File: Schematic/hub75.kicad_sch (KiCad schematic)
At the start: 3 parts, among them J1 Conn_02x08_Odd_Even, J3 Conn_01x04_Pin, U1 74LS08

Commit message: initial CB design
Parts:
- added C6: .1uF, Capacitor_SMD:C_0805_2012Metric_Pad1.18x1.45mm_HandSolder, symbol Device:C
- added LD1: LED_Green, LED_THT:LED_D5.0mm, symbol stm32f091-rescue:LED_Small_ALT-Device
- added R1: 5.1k, Resistor_SMD:R_1206_3216Metric_Pad1.30x1.75mm_HandSolder, symbol Device:R_US
- added R16, R18, R20, R21, R22, R24, R25, R26, R27, R28, R29, R30, R31, R32, R33, R34, R35, R36, R37, R38, R39: 1k, Resistor_SMD:R_1206_3216Metric_Pad1.30x1.75mm_HandSolder, symbol Device:R
- added R17, R19, R23: 0, Resistor_SMD:R_1206_3216Metric_Pad1.30x1.75mm_HandSolder, symbol Device:R
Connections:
- net +3V0: now also C6.1
- net GND: now also C6.2, LD1.1 (K), R17.2, R19.2, R23.2, R34.1, R35.1, R36.1, R37.1, R38.1, R39.1; no longer J1.16 (Pin_16), J1.4 (Pin_4), J1.8 (Pin_8), U1.10, U1.12, U1.13, U1.4, U1.5, U1.9
- net PC0: now also R24.2; no longer J1.1 (Pin_1)
- net PC1: now also R16.2; no longer J1.2 (Pin_2)
- net PC10: now also R29.2; no longer J1.11 (Pin_11)
- net PC11: now also R21.2; no longer J1.12 (Pin_12)
- net PC12: now also R22.2; no longer J1.14 (Pin_14)
- net PC13: now also R31.2; no longer J1.15 (Pin_15)
- net PC2: now also R25.2; no longer J1.3 (Pin_3)
- net PC3: now also R26.2; no longer J1.5 (Pin_5)
- net PC4: now also R18.2; no longer J1.6 (Pin_6)
- net PC5: now also R27.2; no longer J1.7 (Pin_7)
- net PC6: now also R33.1; no longer U1.2
- net PC7: now also R32.1; no longer U1.1
- net PC8: now also R28.2; no longer J1.9 (Pin_9)
- net PC9: now also R20.2; no longer J1.10 (Pin_10)
- net at J1.13 (Pin_13): now also R30.1; no longer U1.3
- new net: R37.2, U1.10
- new net: R36.2, U1.9
- new net: J1.15 (Pin_15), R31.1
- new net: R32.2, U1.1
- new net: J1.3 (Pin_3), R25.1
- new net: J1.6 (Pin_6), R18.1
- new net: J1.16 (Pin_16), R23.1
- new net: R1.1, R30.2, U1.3
- new net: R38.2, U1.12
- new net: R33.2, U1.2
- new net: LD1.2 (A), R1.2
- new net: J1.7 (Pin_7), R27.1
- new net: R34.2, U1.4
- new net: R35.2, U1.5
- new net: J1.14 (Pin_14), R22.1
- new net: J1.2 (Pin_2), R16.1
- new net: R39.2, U1.13
- new net: J1.11 (Pin_11), R29.1
- new net: J1.9 (Pin_9), R28.1
- new net: J1.12 (Pin_12), R21.1
- new net: J1.1 (Pin_1), R24.1
- new net: J1.10 (Pin_10), R20.1
- new net: J1.4 (Pin_4), R17.1
- new net: J1.5 (Pin_5), R26.1
- new net: J1.8 (Pin_8), R19.1
- no-connect marks 0 -> 3
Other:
- note added: "1.8V @ 0.7mA"
- moved on the sheet: J1, J3, U1A, U1B, U1C, U1D, U1E

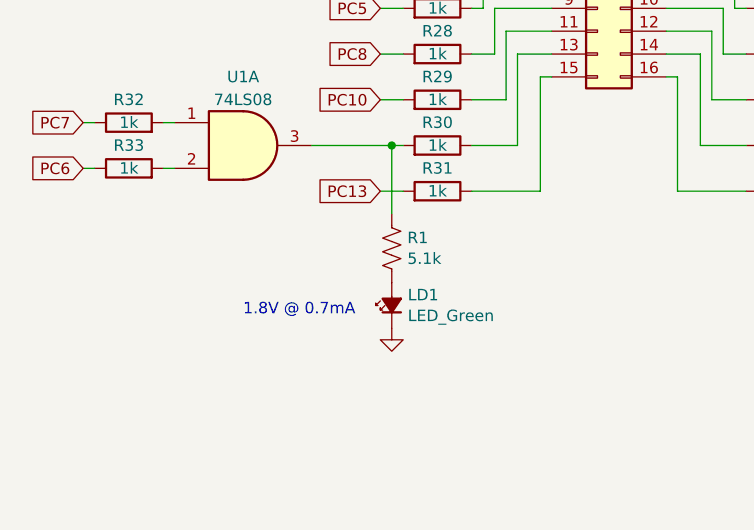
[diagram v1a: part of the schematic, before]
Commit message: Most of the schematic and PCB layout.
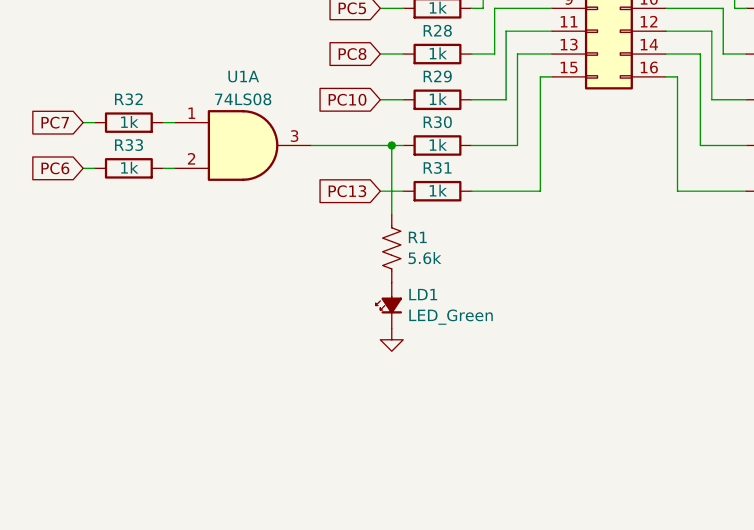
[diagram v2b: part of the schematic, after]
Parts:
- R1: value 5.1k -> 5.6k
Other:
- note removed: "1.8V @ 0.7mA"
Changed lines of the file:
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@@
     (stroke (width 0) (type default))
-  )
-  (text "1.8V @ 0.7mA" (at 43.18 72.39 0)
-    (effects (font (size 1.27 1.27)) (justify left bottom))
   )
   (global_label "PC12" (shape input) (at 109.22 53.34 0) (fields_autoplaced)
@@
       (effects (font (size 1.27 1.27)) (justify left))
     )
-    (property "Value" "5.1k" (at 61.4172 65.913 0)
+    (property "Value" "5.6k" (at 61.4172 65.913 0)
       (effects (font (size 1.27 1.27)) (justify left))
     )

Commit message: Added stuff from today
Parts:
- removed unit 1 of U1
- removed unit 2 of U1
- added J10, J11, J12, J13, J14, J15, J16, J7, J8, J9: Conn_01x03_Pin, Connector_PinSocket_2.54mm:PinSocket_1x03_P2.54mm_Vertical, symbol Connector:Conn_01x03_Pin
- added R45, R46: 1k, Resistor_SMD:R_1206_3216Metric_Pad1.30x1.75mm_HandSolder, symbol Device:R
- added unit 2 of U1 (x2)
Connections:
- net GND: no longer R38.1, R39.1
- net at R37.2: now also U1.13, R45.2; no longer U1.10
- net PB15: now reaches U1.8
- net at R36.2: now also U1.12, R46.2; no longer U1.9
- net at R32.2: now also U1.4
- net at R1.1, R30.2: now also U1.6
- net at R38.2: now also R35.2, U1.5; no longer U1.12
- net at R33.2: now also U1.5
- net at R34.2: now also R39.2, U1.4
- net at U1.11: now also U1.10
- new net: U1.6, U1.9
- no-connect marks 3 -> 0

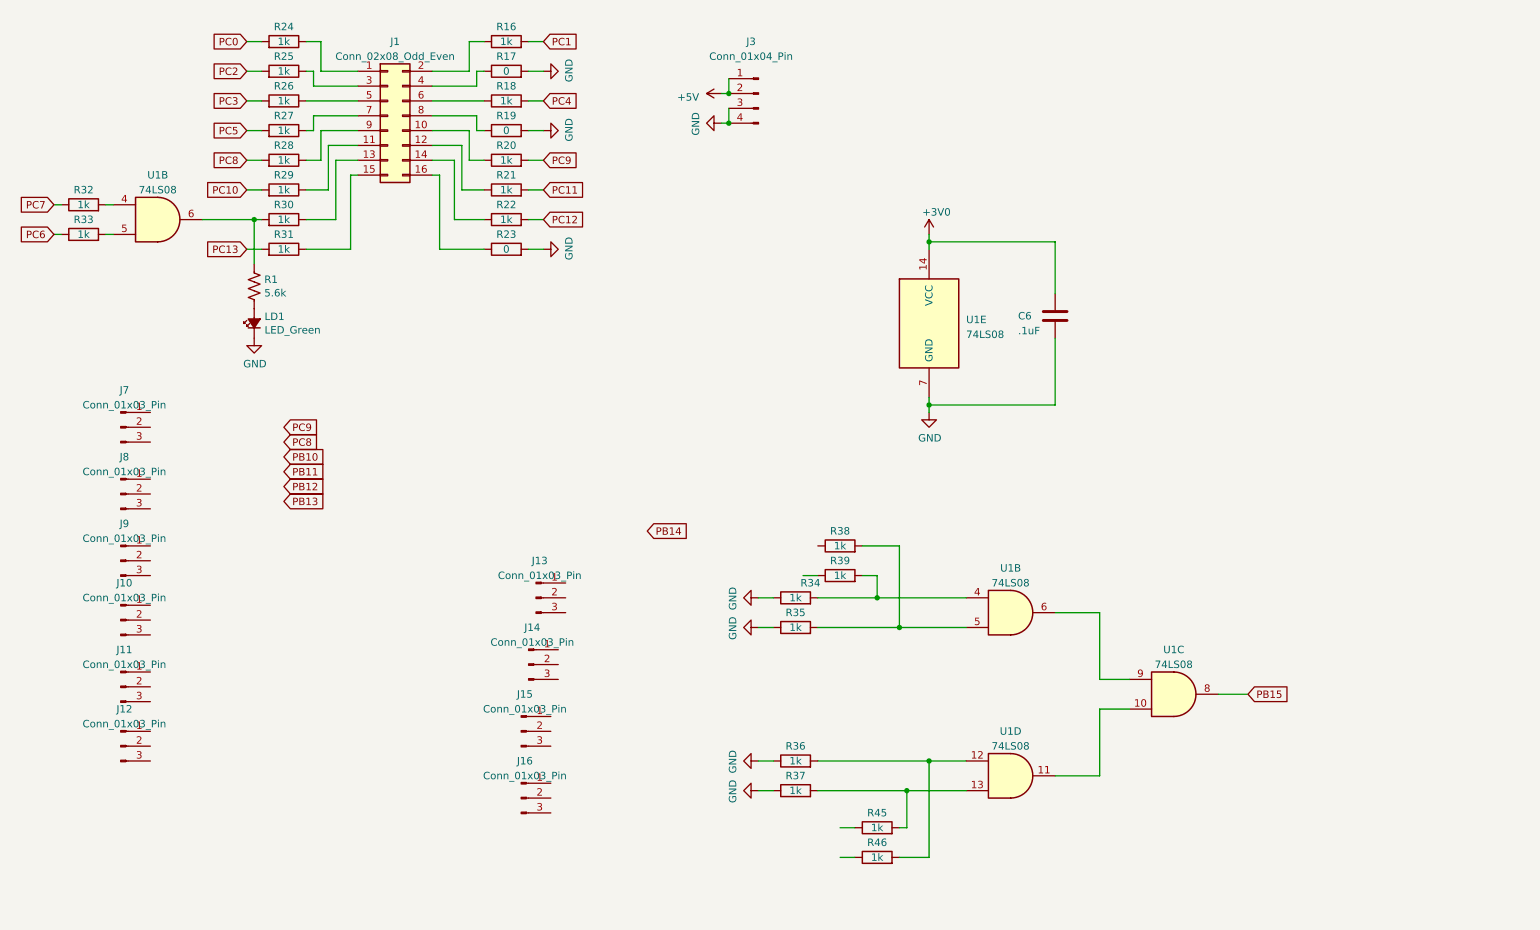
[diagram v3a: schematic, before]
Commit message: Added sensors. Fixed other stuff.
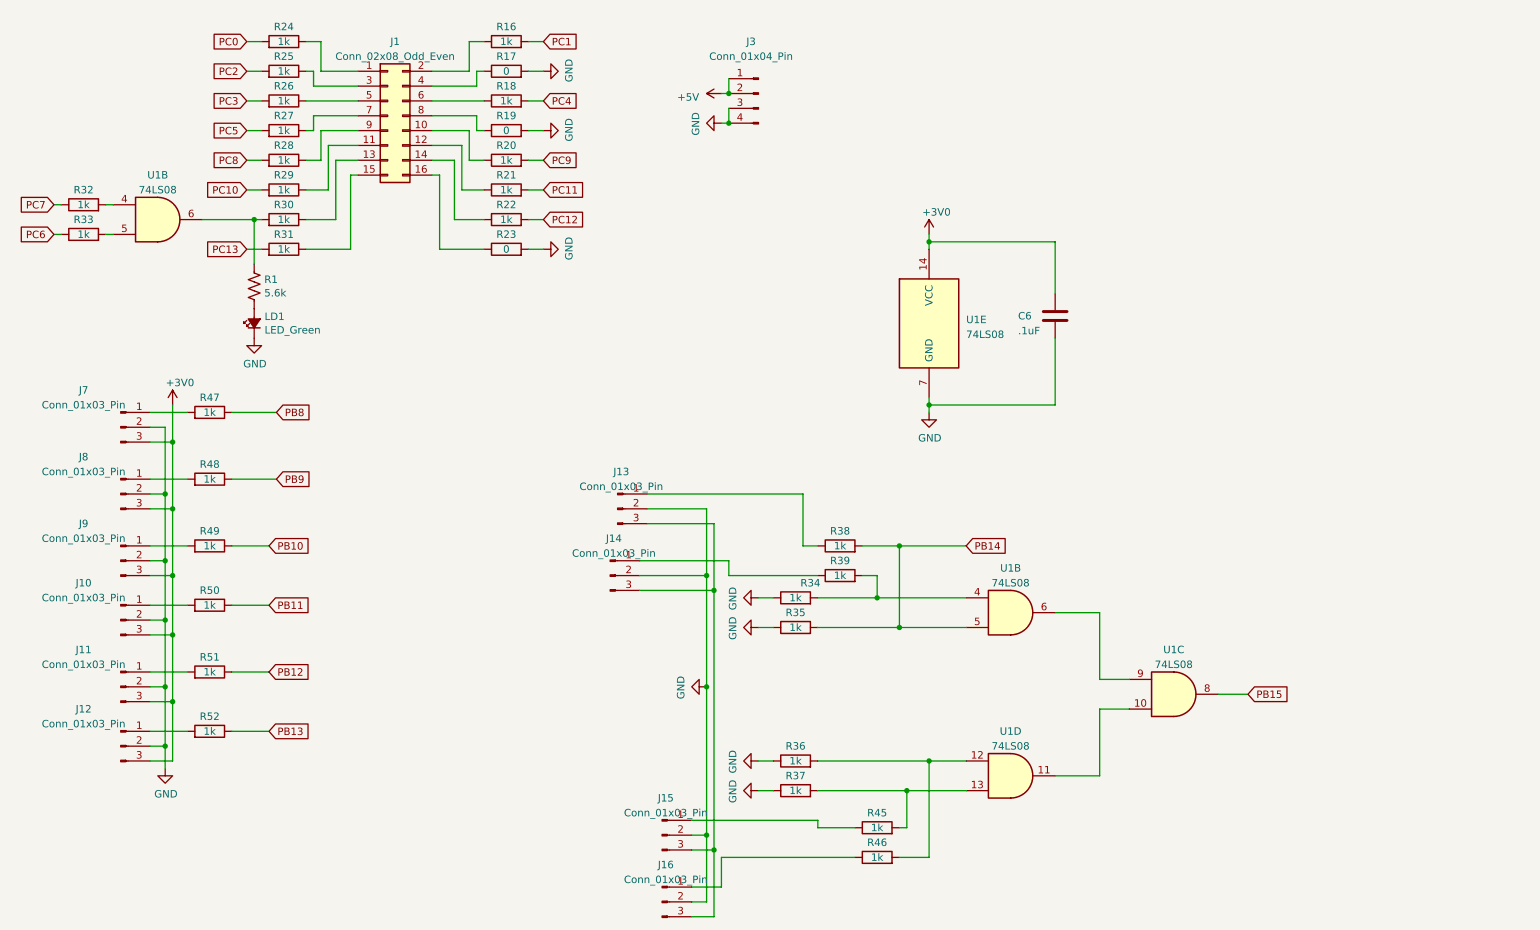
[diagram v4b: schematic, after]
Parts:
- added R47, R48, R49, R50, R51, R52: 1k, Resistor_SMD:R_1206_3216Metric_Pad1.30x1.75mm_HandSolder, symbol Device:R
- J10, J11, J12, J13, J14, J15, J16, J7, J8, J9: footprint Connector_PinSocket_2.54mm:PinSocket_1x03_P2.54mm_Vertical -> Connector_JST:JST_VH_B3P-VH_1x03_P3.96mm_Vertical
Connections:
- net +3V0: now also J10.3 (Pin_3), J11.3 (Pin_3), J12.3 (Pin_3), J7.3 (Pin_3), J8.3 (Pin_3), J9.3 (Pin_3)
- net GND: now also J10.2 (Pin_2), J11.2 (Pin_2), J12.2 (Pin_2), J13.2 (Pin_2), J14.2 (Pin_2), J15.2 (Pin_2), J16.2 (Pin_2), J7.2 (Pin_2), J8.2 (Pin_2), J9.2 (Pin_2)
- net PB10: now also R49.1
- net PB11: now also R50.1
- net PB12: now also R51.1
- net PB13: now also R52.1
- net PB14: now also R35.2, R38.2, U1.5
- net at R39.1: now also J14.1 (Pin_1)
- net at J15.1 (Pin_1): now also R45.1
- net at J15.3 (Pin_3): now also J13.3 (Pin_3), J14.3 (Pin_3), J16.3 (Pin_3)
- net at J8.1 (Pin_1): now also R48.2
- net at J12.1 (Pin_1): now also R52.2
- net at J16.1 (Pin_1): now also R46.1
- net at J10.1 (Pin_1): now also R50.2
- net at J11.1 (Pin_1): now also R51.2
- net at J7.1 (Pin_1): now also R47.2
- net at J9.1 (Pin_1): now also R49.2
- net at J13.1 (Pin_1): now also R38.1
- new net PB8: R47.1
- new net PB9: R48.1
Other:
- moved on the sheet: J13, J14, J15, J16

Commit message: Mostly finallized PCB
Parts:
- added J20: WS2812B_DATA, Connector_JST:JST_VH_B2P-VH-B_1x02_P3.96mm_Vertical, symbol Connector_Generic:Conn_01x02
- added J21: WS2812B_PWR, Connector_JST:JST_VH_B2P-VH-B_1x02_P3.96mm_Vertical, symbol Connector_Generic:Conn_01x02
- added R55, R58, R59, R60, R61, R62, R63, R64, R65, R66: 2k, Resistor_SMD:R_1206_3216Metric_Pad1.30x1.75mm_HandSolder, symbol Device:R
- added R67: 7.5k, LED_SMD:LED_1206_3216Metric_Pad1.42x1.75mm_HandSolder, symbol Device:R
- added R68: 3k, LED_SMD:LED_1206_3216Metric_Pad1.42x1.75mm_HandSolder, symbol Device:R
- J1: value Conn_02x08_Odd_Even -> HUB75_DATA
- J3: value Conn_01x04_Pin -> HUB75_PWR
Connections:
- net +3V0: no longer J10.3 (Pin_3), J11.3 (Pin_3), J12.3 (Pin_3), J7.3 (Pin_3), J8.3 (Pin_3), J9.3 (Pin_3)
- net +5V: now also J10.3 (Pin_3), J11.3 (Pin_3), J12.3 (Pin_3), J13.3 (Pin_3), J14.3 (Pin_3), J15.3 (Pin_3), J16.3 (Pin_3), J7.3 (Pin_3), J8.3 (Pin_3), J9.3 (Pin_3), J21.1 (Pin_1), R67.1
- net GND: now also J20.2 (Pin_2), J21.2 (Pin_2), R55.2, R58.2, R59.2, R60.2, R61.2, R62.2, R63.2, R64.2, R65.2, R66.2
- net PB10: now also R59.1
- net PB11: now also R60.1
- net PB12: now also R61.1
- net PB13: now also R66.1
- net PB8: now also R55.1
- net PB9: now also R58.1
- net at R34.2, R39.2, U1.4: now also R65.1
- net at R37.2, R45.2, U1.13: now also R63.1
- net at R36.2, R46.2, U1.12: now also R62.1
- net PB14: no longer names the net of R35.2, R38.2, U1.5
- net PB14: now also R64.1
- new net: J20.1 (Pin_1), R67.2, R68.1
- new net PA7: R68.2
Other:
- moved on the sheet: J10, J11, J12, R45, R46, R50, R51, R52

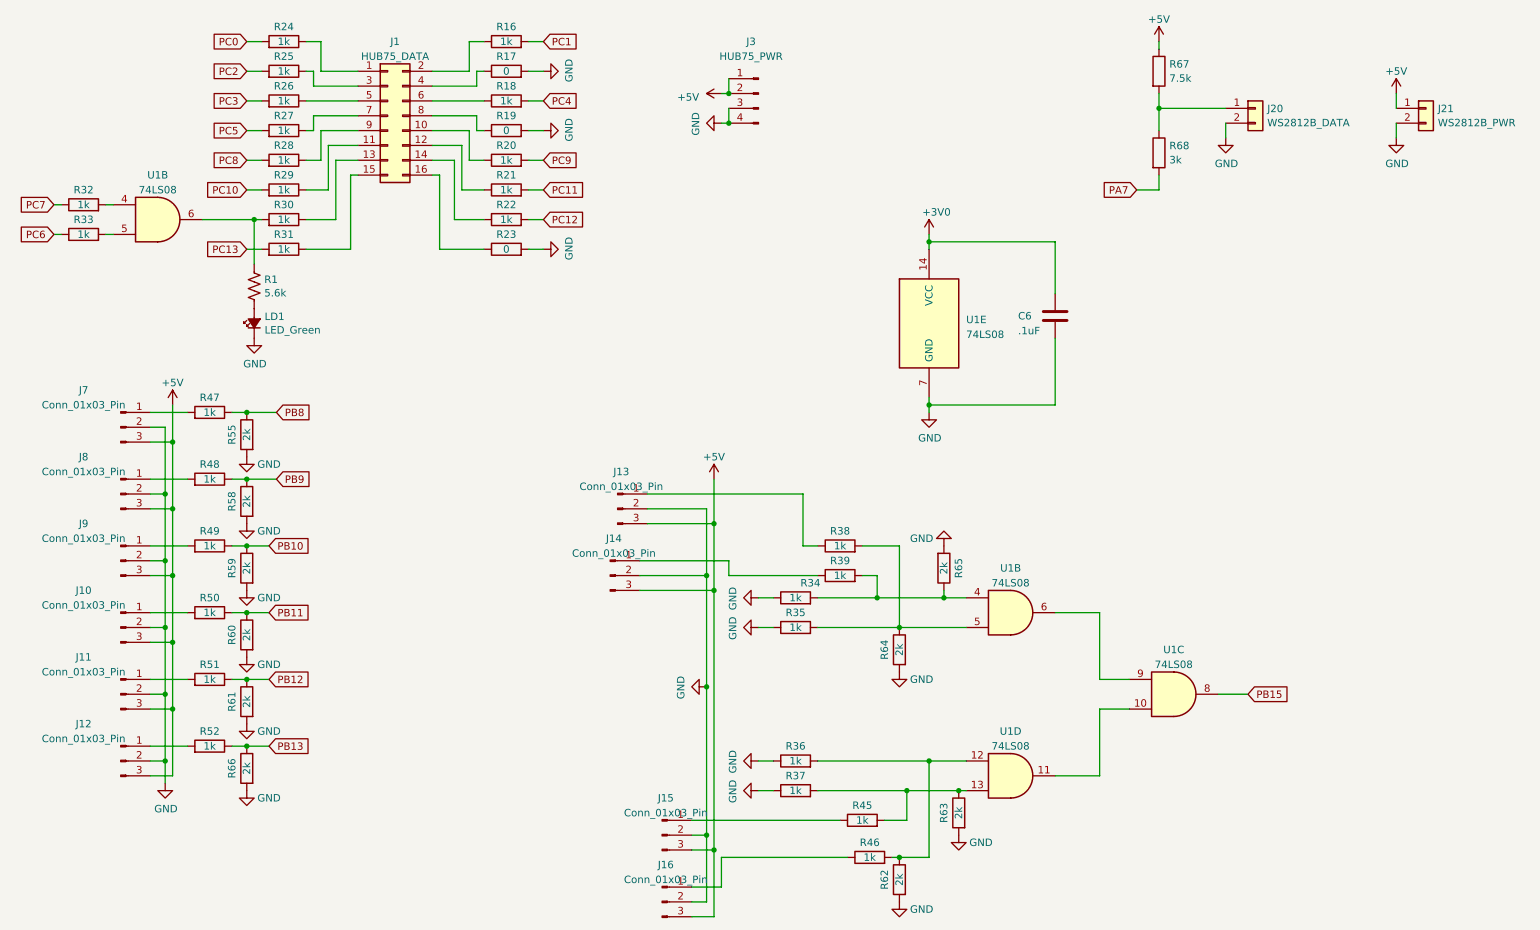
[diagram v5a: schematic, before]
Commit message: Added images
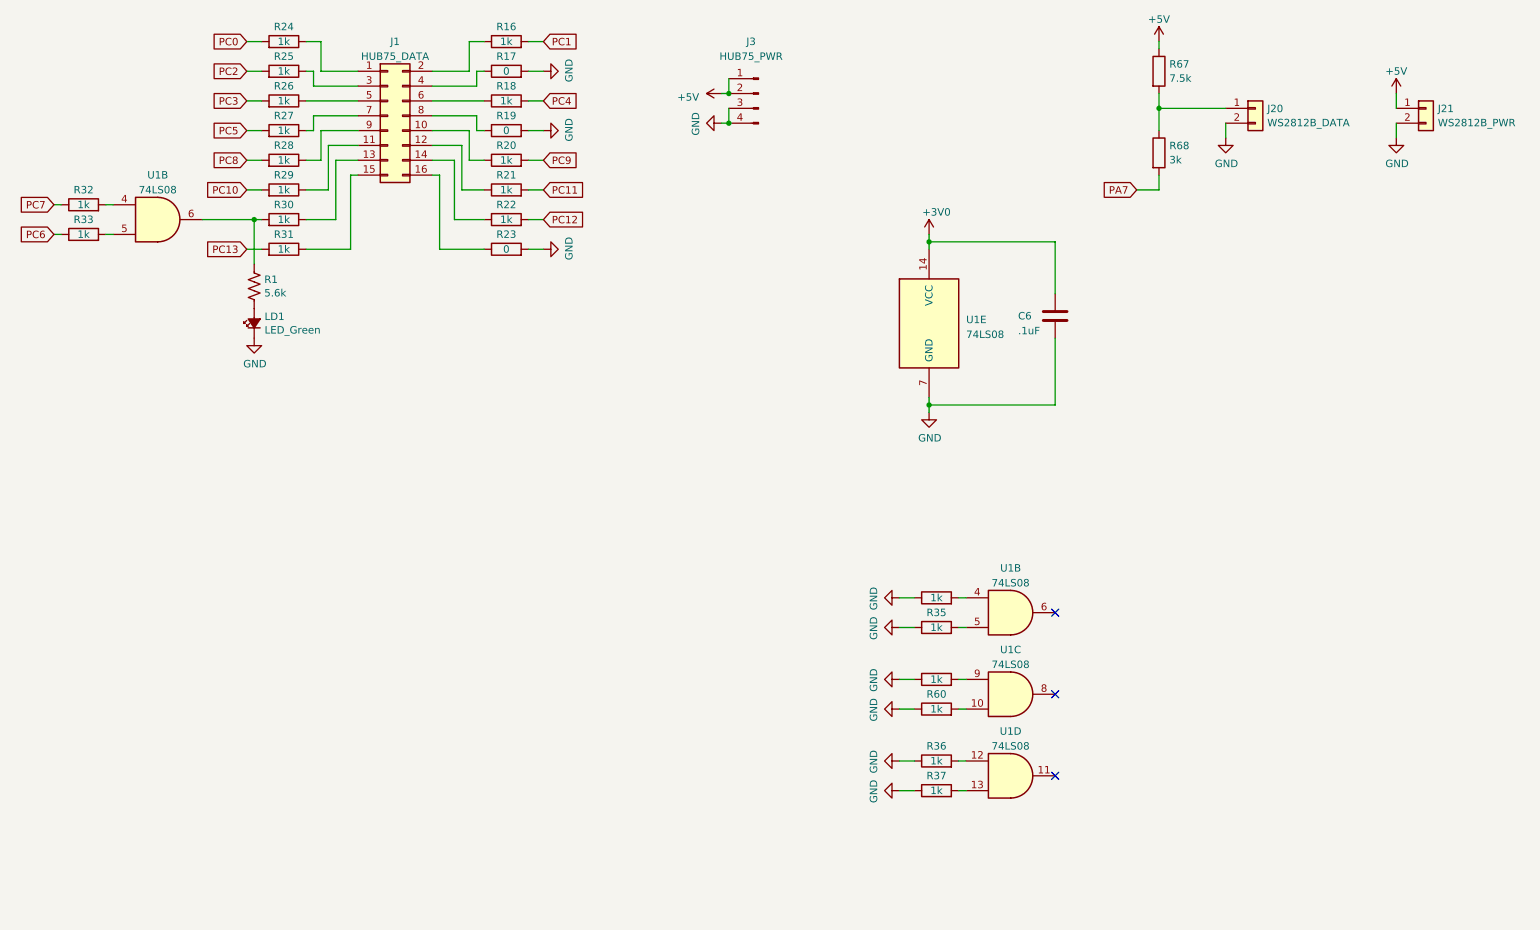
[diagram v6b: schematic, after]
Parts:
- removed J10, J11, J12, J13, J14, J15, J16, J7, J8, J9: Conn_01x03_Pin, Connector_JST:JST_VH_B3P-VH_1x03_P3.96mm_Vertical, symbol Connector:Conn_01x03_Pin
- removed R38, R39, R45, R46, R47, R48, R49, R50, R51, R52: 1k, Resistor_SMD:R_1206_3216Metric_Pad1.30x1.75mm_HandSolder, symbol Device:R
- removed R55, R58, R61, R62, R63, R64, R65, R66: 2k, Resistor_SMD:R_1206_3216Metric_Pad1.30x1.75mm_HandSolder, symbol Device:R
- R59, R60: value 2k -> 1k
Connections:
- net PB10 is gone; now on net GND: R59.1
- net PB11 is gone; now on net GND: R60.1
- net GND: no longer R59.2, R60.2
- net at U1.11: no longer U1.10
- net at U1.9: now also R59.2; no longer U1.6
- net PB15: no longer names the net of U1.8
- new net: R60.2, U1.10
- no-connect marks 0 -> 3
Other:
- moved on the sheet: R35, R36, R37, U1C

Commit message: Added Cap to osilator, and fixed posible issues with signals near it.
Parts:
- C6: footprint Capacitor_SMD:C_0805_2012Metric_Pad1.18x1.45mm_HandSolder -> Capacitor_SMD:C_1206_3216Metric_Pad1.33x1.80mm_HandSolder
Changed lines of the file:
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@@
       (effects (font (size 1.27 1.27)) (justify left))
     )
-    (property "Footprint" "Capacitor_SMD:C_0805_2012Metric_Pad1.18x1.45mm_HandSolder" (at 197.8152 73.66 0)
+    (property "Footprint" "Capacitor_SMD:C_1206_3216Metric_Pad1.33x1.80mm_HandSolder" (at 197.8152 73.66 0)
       (effects (font (size 1.27 1.27)) hide)
     )

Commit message: Forgot to save the schematic from the last commit.
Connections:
- net PA7 renamed PA3
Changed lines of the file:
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@@
     )
   )
-  (global_label "PA7" (shape input) (at 210.82 48.26 180) (fields_autoplaced)
+  (global_label "PA3" (shape input) (at 210.82 48.26 180) (fields_autoplaced)
     (effects (font (size 1.27 1.27)) (justify right))
-    (property "Intersheetrefs" "${INTERSHEET_REFS}" (at 204.2667 48.26 0)
+    (property "Intersheetrefs" "${INTERSHEET_REFS}" (at 204.3461 48.26 0)
       (effects (font (size 1.27 1.27)) (justify right) hide)
     )
